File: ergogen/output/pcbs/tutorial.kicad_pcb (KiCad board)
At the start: 2 copper layers, 135 x 96 mm, 41 parts

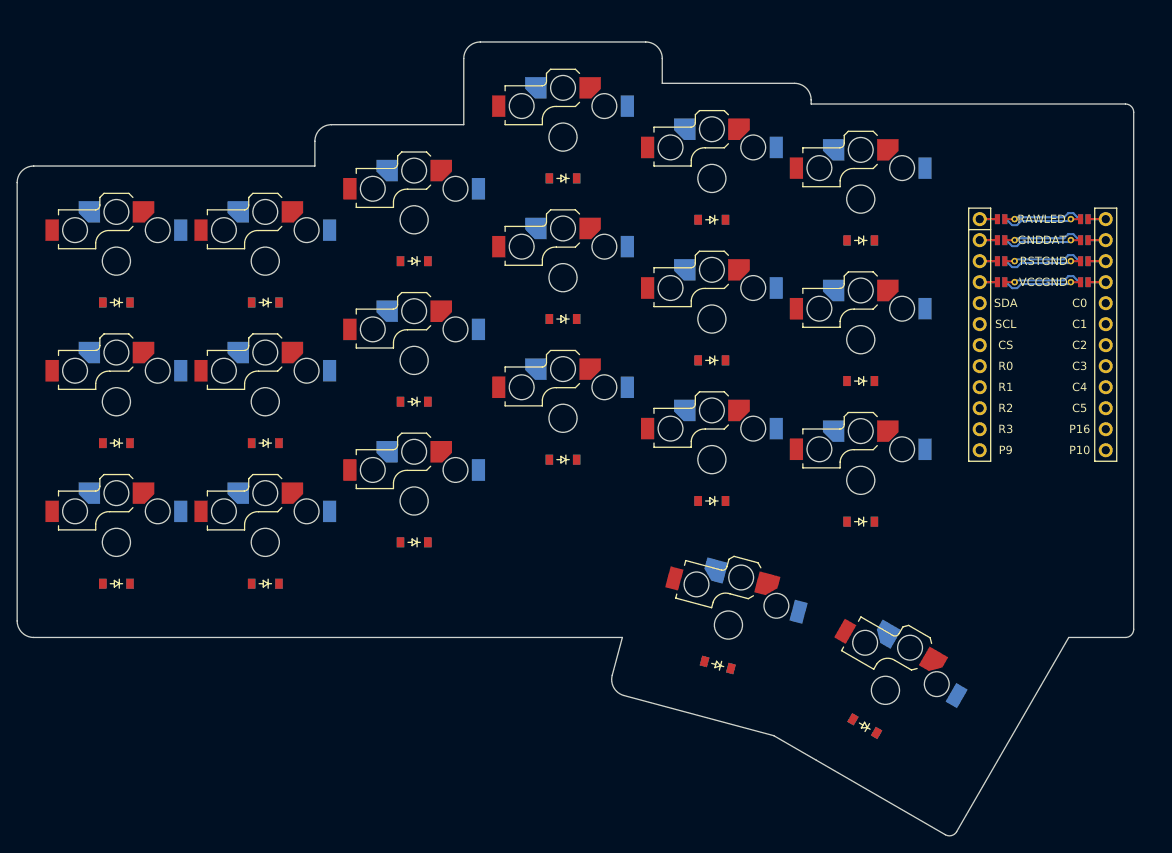
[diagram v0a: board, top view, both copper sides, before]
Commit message: feat: refine layout, add battery connector
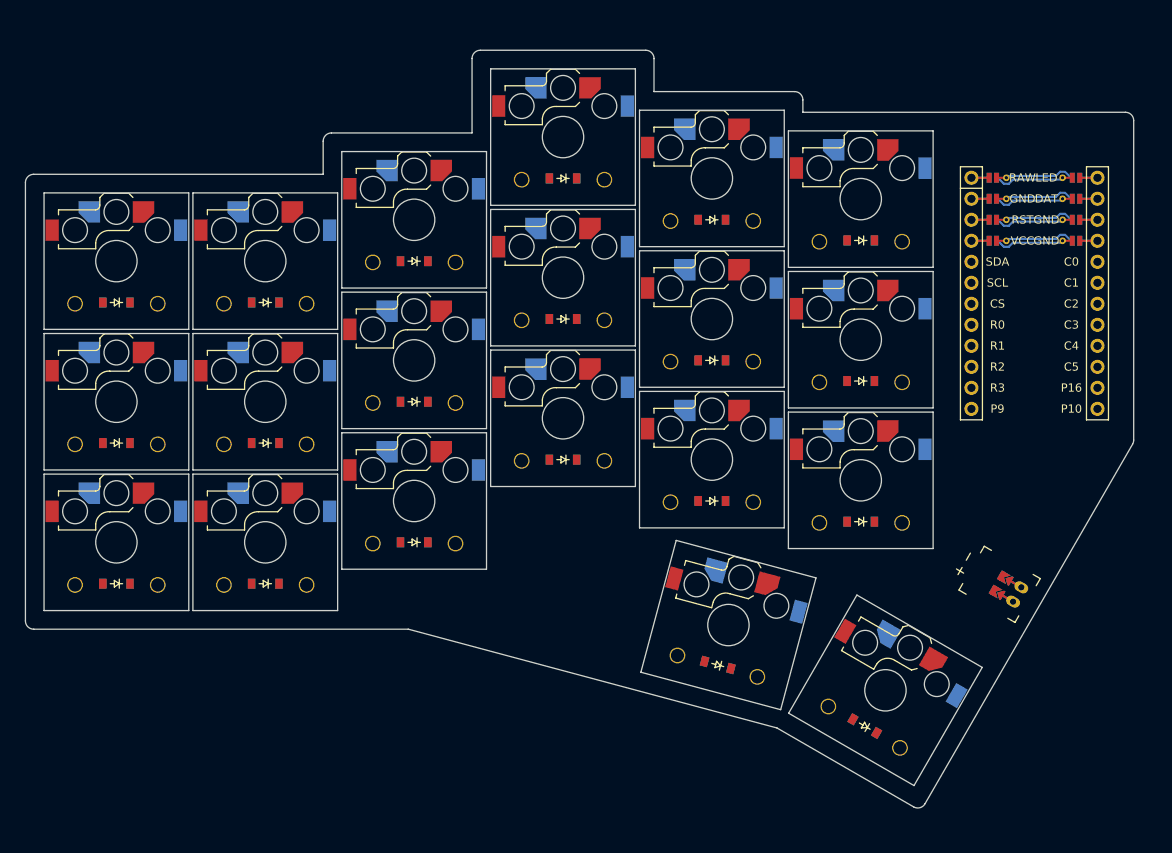
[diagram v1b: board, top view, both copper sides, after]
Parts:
- added JST1: , ceoloide:battery_connector_jst_ph_2, F.Cu at (208.9, 106.3)
- moved MCU1 5.10 mm to (211.0, 68.6)
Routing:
- net JST1_1: track 0.00 -> 3.60 mm
- net JST1_2: track 0.00 -> 3.60 mm
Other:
- board size 135 x 96 mm -> 134 x 91.6 mm

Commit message: feat: add reset button, on/off switch
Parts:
- added PWR1: , ceoloide:power_switch_smd_side, F.Cu at (212.3, 102.5)
- added RST1: , ceoloide:reset_switch_tht_top, F.Cu at (211.0, 90.0)
- moved JST1 5.00 mm to (206.4, 110.6)
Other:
- outline, holes or cut-outs redrawn

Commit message: feat: ceoloide suggestions
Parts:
- moved MCU1 8.22 mm to (215.1, 61.5)
- moved RST1 7.69 mm to (215.1, 83.5)
- moved JST1 7.59 mm to (200.1, 106.4), turned to 60 degrees
- moved D18 6.40 mm to (195.0, 59.5)
- moved S18 6.40 mm to (195.0, 54.5)
- moved D15 5.66 mm to (176.0, 57.0)
- moved S15 5.66 mm to (176.0, 52.0)
- moved PWR1 5.64 mm to (217.7, 103.9)
- moved D20 5.46 mm to (195.5, 124.5)
- moved S20 5.46 mm to (198.0, 120.1)
- moved D17 5.39 mm to (195.0, 78.5)
- moved S17 5.39 mm to (195.0, 73.5)
- moved D12 5.00 mm to (157.0, 52.0)
- moved D16 5.00 mm to (195.0, 97.5)
- moved S12 5.00 mm to (157.0, 47.0)
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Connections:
- net CS renamed P4
- net DAT renamed P0
- net LED renamed P1
- net SCL renamed P3
- net SDA renamed P2
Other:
- board size 134 x 91.6 mm -> 136.1 x 97.6 mm

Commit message: feat: reformat, spacing
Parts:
- moved PWR1 4.50 mm to (220.0, 100.0)
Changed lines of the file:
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@@
       (net 1 "C0")
     )
-    (pad "2" smd rect (at 7.775 -3.75 0) (size 1.6 2.6) (layers "B.Cu" "B.Paste" "B.Mask") (net 2 "outer_bottom"))
+    (pad "2" smd rect (at 7.9750000000000005 -3.75 0) (size 2 2.6) (layers "B.Cu" "B.Paste" "B.Mask") (net 2 "outer_bottom"))
     (pad "" np_thru_hole circle (at 5 -3.75 195) (size 3 3) (drill 3) (layers "*.Cu" "*.Mask"))
   )
@@
       (net 1 "C0")
     )
-    (pad "2" smd rect (at 7.775 -3.75 0) (size 1.6 2.6) (layers "B.Cu" "B.Paste" "B.Mask") (net 6 "outer_home"))
+    (pad "2" smd rect (at 7.9750000000000005 -3.75 0) (size 2 2.6) (layers "B.Cu" "B.Paste" "B.Mask") (net 6 "outer_home"))
     (pad "" np_thru_hole circle (at 5 -3.75 195) (size 3 3) (drill 3) (layers "*.Cu" "*.Mask"))
   )
@@
       (net 1 "C0")
     )
-    (pad "2" smd rect (at 7.775 -3.75 0) (size 1.6 2.6) (layers "B.Cu" "B.Paste" "B.Mask") (net 7 "outer_top"))
+    (pad "2" smd rect (at 7.9750000000000005 -3.75 0) (size 2 2.6) (layers "B.Cu" "B.Paste" "B.Mask") (net 7 "outer_top"))
     (pad "" np_thru_hole circle (at 5 -3.75 195) (size 3 3) (drill 3) (layers "*.Cu" "*.Mask"))
   )
@@
       (net 8 "C1")
     )
-    (pad "2" smd rect (at 7.775 -3.75 0) (size 1.6 2.6) (layers "B.Cu" "B.Paste" "B.Mask") (net 9 "pinky_bottom"))
+    (pad "2" smd rect (at 7.9750000000000005 -3.75 0) (size 2 2.6) (layers "B.Cu" "B.Paste" "B.Mask") (net 9 "pinky_bottom"))
     (pad "" np_thru_hole circle (at 5 -3.75 195) (size 3 3) (drill 3) (layers "*.Cu" "*.Mask"))
   )
@@
       (net 8 "C1")
     )
-    (pad "2" smd rect (at 7.775 -3.75 0) (size 1.6 2.6) (layers "B.Cu" "B.Paste" "B.Mask") (net 10 "pinky_home"))
+    (pad "2" smd rect (at 7.9750000000000005 -3.75 0) (size 2 2.6) (layers "B.Cu" "B.Paste" "B.Mask") (net 10 "pinky_home"))
     (pad "" np_thru_hole circle (at 5 -3.75 195) (size 3 3) (drill 3) (layers "*.Cu" "*.Mask"))
   )
@@
       (net 8 "C1")
     )
-    (pad "2" smd rect (at 7.775 -3.75 0) (size 1.6 2.6) (layers "B.Cu" "B.Paste" "B.Mask") (net 11 "pinky_top"))
+    (pad "2" smd rect (at 7.9750000000000005 -3.75 0) (size 2 2.6) (layers "B.Cu" "B.Paste" "B.Mask") (net 11 "pinky_top"))
     (pad "" np_thru_hole circle (at 5 -3.75 195) (size 3 3) (drill 3) (layers "*.Cu" "*.Mask"))
   )
@@
       (net 12 "C2")
     )
-    (pad "2" smd rect (at 7.775 -3.75 0) (size 1.6 2.6) (layers "B.Cu" "B.Paste" "B.Mask") (net 13 "ring_bottom"))
+    (pad "2" smd rect (at 7.9750000000000005 -3.75 0) (size 2 2.6) (layers "B.Cu" "B.Paste" "B.Mask") (net 13 "ring_bottom"))
     (pad "" np_thru_hole circle (at 5 -3.75 195) (size 3 3) (drill 3) (layers "*.Cu" "*.Mask"))
   )
@@
       (net 12 "C2")
     )
-    (pad "2" smd rect (at 7.775 -3.75 0) (size 1.6 2.6) (layers "B.Cu" "B.Paste" "B.Mask") (net 14 "ring_home"))
+    (pad "2" smd rect (at 7.9750000000000005 -3.75 0) (size 2 2.6) (layers "B.Cu" "B.Paste" "B.Mask") (net 14 "ring_home"))
     (pad "" np_thru_hole circle (at 5 -3.75 195) (size 3 3) (drill 3) (layers "*.Cu" "*.Mask"))
   )
@@
       (net 12 "C2")
     )
-    (pad "2" smd rect (at 7.775 -3.75 0) (size 1.6 2.6) (layers "B.Cu" "B.Paste" "B.Mask") (net 15 "ring_top"))
+    (pad "2" smd rect (at 7.9750000000000005 -3.75 0) (size 2 2.6) (layers "B.Cu" "B.Paste" "B.Mask") (net 15 "ring_top"))
     (pad "" np_thru_hole circle (at 5 -3.75 195) (size 3 3) (drill 3) (layers "*.Cu" "*.Mask"))
   )
@@
       (net 16 "C3")
     )
-    (pad "2" smd rect (at 7.775 -3.75 0) (size 1.6 2.6) (layers "B.Cu" "B.Paste" "B.Mask") (net 17 "middle_bottom"))
+    (pad "2" smd rect (at 7.9750000000000005 -3.75 0) (size 2 2.6) (layers "B.Cu" "B.Paste" "B.Mask") (net 17 "middle_bottom"))
     (pad "" np_thru_hole circle (at 5 -3.75 195) (size 3 3) (drill 3) (layers "*.Cu" "*.Mask"))
   )
@@
       (net 16 "C3")
     )
-    (pad "2" smd rect (at 7.775 -3.75 0) (size 1.6 2.6) (layers "B.Cu" "B.Paste" "B.Mask") (net 18 "middle_home"))
+    (pad "2" smd rect (at 7.9750000000000005 -3.75 0) (size 2 2.6) (layers "B.Cu" "B.Paste" "B.Mask") (net 18 "middle_home"))
     (pad "" np_thru_hole circle (at 5 -3.75 195) (size 3 3) (drill 3) (layers "*.Cu" "*.Mask"))
   )
@@
       (net 16 "C3")
     )
-    (pad "2" smd rect (at 7.775 -3.75 0) (size 1.6 2.6) (layers "B.Cu" "B.Paste" "B.Mask") (net 19 "middle_top"))
+    (pad "2" smd rect (at 7.9750000000000005 -3.75 0) (size 2 2.6) (layers "B.Cu" "B.Paste" "B.Mask") (net 19 "middle_top"))
     (pad "" np_thru_hole circle (at 5 -3.75 195) (size 3 3) (drill 3) (layers "*.Cu" "*.Mask"))
   )
@@
       (net 20 "C4")
     )
-    (pad "2" smd rect (at 7.775 -3.75 0) (size 1.6 2.6) (layers "B.Cu" "B.Paste" "B.Mask") (net 21 "index_bottom"))
+    (pad "2" smd rect (at 7.9750000000000005 -3.75 0) (size 2 2.6) (layers "B.Cu" "B.Paste" "B.Mask") (net 21 "index_bottom"))
     (pad "" np_thru_hole circle (at 5 -3.75 195) (size 3 3) (drill 3) (layers "*.Cu" "*.Mask"))
   )
@@
       (net 20 "C4")
     )
-    (pad "2" smd rect (at 7.775 -3.75 0) (size 1.6 2.6) (layers "B.Cu" "B.Paste" "B.Mask") (net 22 "index_home"))
+    (pad "2" smd rect (at 7.9750000000000005 -3.75 0) (size 2 2.6) (layers "B.Cu" "B.Paste" "B.Mask") (net 22 "index_home"))
     (pad "" np_thru_hole circle (at 5 -3.75 195) (size 3 3) (drill 3) (layers "*.Cu" "*.Mask"))
   )
@@
       (net 20 "C4")
     )
-    (pad "2" smd rect (at 7.775 -3.75 0) (size 1.6 2.6) (layers "B.Cu" "B.Paste" "B.Mask") (net 23 "index_top"))
+    (pad "2" smd rect (at 7.9750000000000005 -3.75 0) (size 2 2.6) (layers "B.Cu" "B.Paste" "B.Mask") (net 23 "index_top"))
     (pad "" np_thru_hole circle (at 5 -3.75 195) (size 3 3) (drill 3) (layers "*.Cu" "*.Mask"))
   )
@@
       (net 24 "C5")
     )
-    (pad "2" smd rect (at 7.775 -3.75 0) (size 1.6 2.6) (layers "B.Cu" "B.Paste" "B.Mask") (net 25 "indexfar_bottom"))
+    (pad "2" smd rect (at 7.9750000000000005 -3.75 0) (size 2 2.6) (layers "B.Cu" "B.Paste" "B.Mask") (net 25 "indexfar_bottom"))
     (pad "" np_thru_hole circle (at 5 -3.75 195) (size 3 3) (drill 3) (layers "*.Cu" "*.Mask"))
   )
@@
       (net 24 "C5")
     )
-    (pad "2" smd rect (at 7.775 -3.75 0) (size 1.6 2.6) (layers "B.Cu" "B.Paste" "B.Mask") (net 26 "indexfar_home"))
+    (pad "2" smd rect (at 7.9750000000000005 -3.75 0) (size 2 2.6) (layers "B.Cu" "B.Paste" "B.Mask") (net 26 "indexfar_home"))
     (pad "" np_thru_hole circle (at 5 -3.75 195) (size 3 3) (drill 3) (layers "*.Cu" "*.Mask"))
   )
@@
       (net 24 "C5")
     )
-    (pad "2" smd rect (at 7.775 -3.75 0) (size 1.6 2.6) (layers "B.Cu" "B.Paste" "B.Mask") (net 27 "indexfar_top"))
+    (pad "2" smd rect (at 7.9750000000000005 -3.75 0) (size 2 2.6) (layers "B.Cu" "B.Paste" "B.Mask") (net 27 "indexfar_top"))
     (pad "" np_thru_hole circle (at 5 -3.75 195) (size 3 3) (drill 3) (layers "*.Cu" "*.Mask"))
   )
@@
       (net 20 "C4")
     )
-    (pad "2" smd rect (at 7.775 -3.75 -15) (size 1.6 2.6) (layers "B.Cu" "B.Paste" "B.Mask") (net 28 "layer_cluster"))
+    (pad "2" smd rect (at 7.9750000000000005 -3.75 -15) (size 2 2.6) (layers "B.Cu" "B.Paste" "B.Mask") (net 28 "layer_cluster"))
     (pad "" np_thru_hole circle (at 5 -3.75 180) (size 3 3) (drill 3) (layers "*.Cu" "*.Mask"))
   )
@@
       (net 24 "C5")
     )
-    (pad "2" smd rect (at 7.775 -3.75 -30) (size 1.6 2.6) (layers "B.Cu" "B.Paste" "B.Mask") (net 29 "space_cluster"))
+    (pad "2" smd rect (at 7.9750000000000005 -3.75 -30) (size 2 2.6) (layers "B.Cu" "B.Paste" "B.Mask") (net 29 "space_cluster"))
     (pad "" np_thru_hole circle (at 5 -3.75 165) (size 3 3) (drill 3) (layers "*.Cu" "*.Mask"))
   )
@@
   (footprint "ceoloide:power_switch_smd_side"
     (layer "F.Cu")
-    (at 217.7448955 103.86500299999999 -30)
+    (at 219.9948955 99.96788869999999 -30)
     (property "Reference" "PWR1"
       (at -3.6 0 -120)
